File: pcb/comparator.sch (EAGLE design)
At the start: 13 parts, among them U1 MAX9032

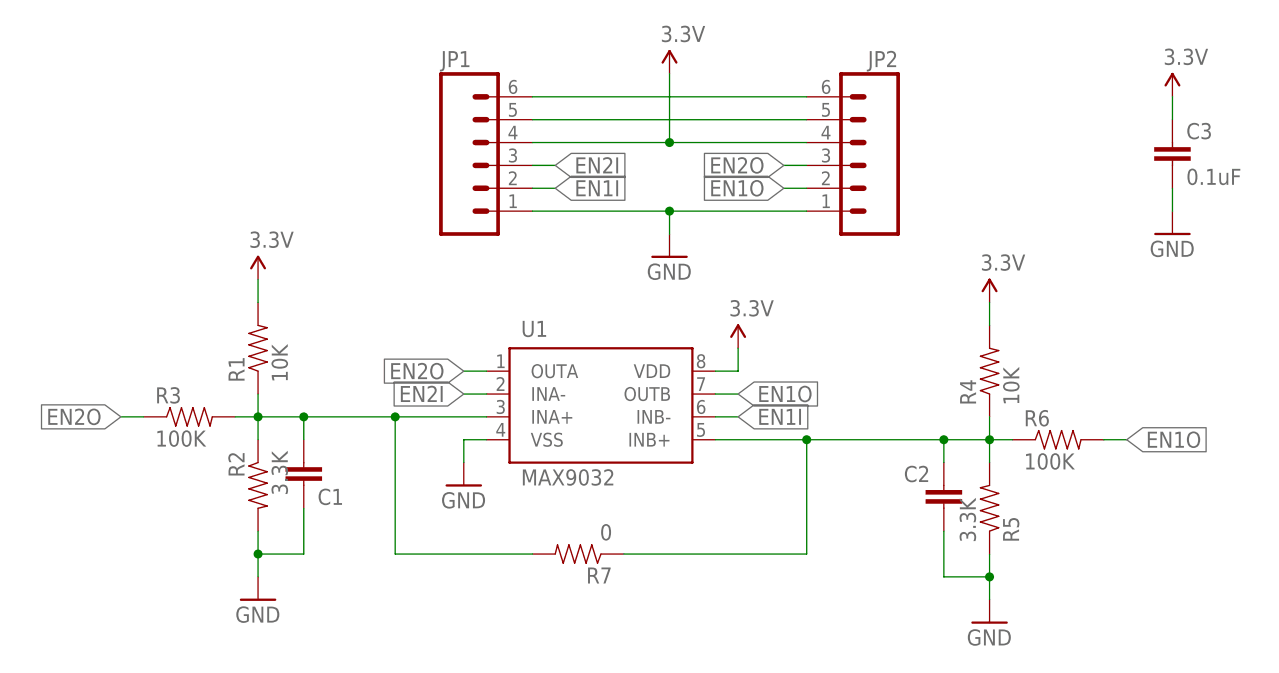
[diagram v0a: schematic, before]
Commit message: Tweaked encoder conditiner board
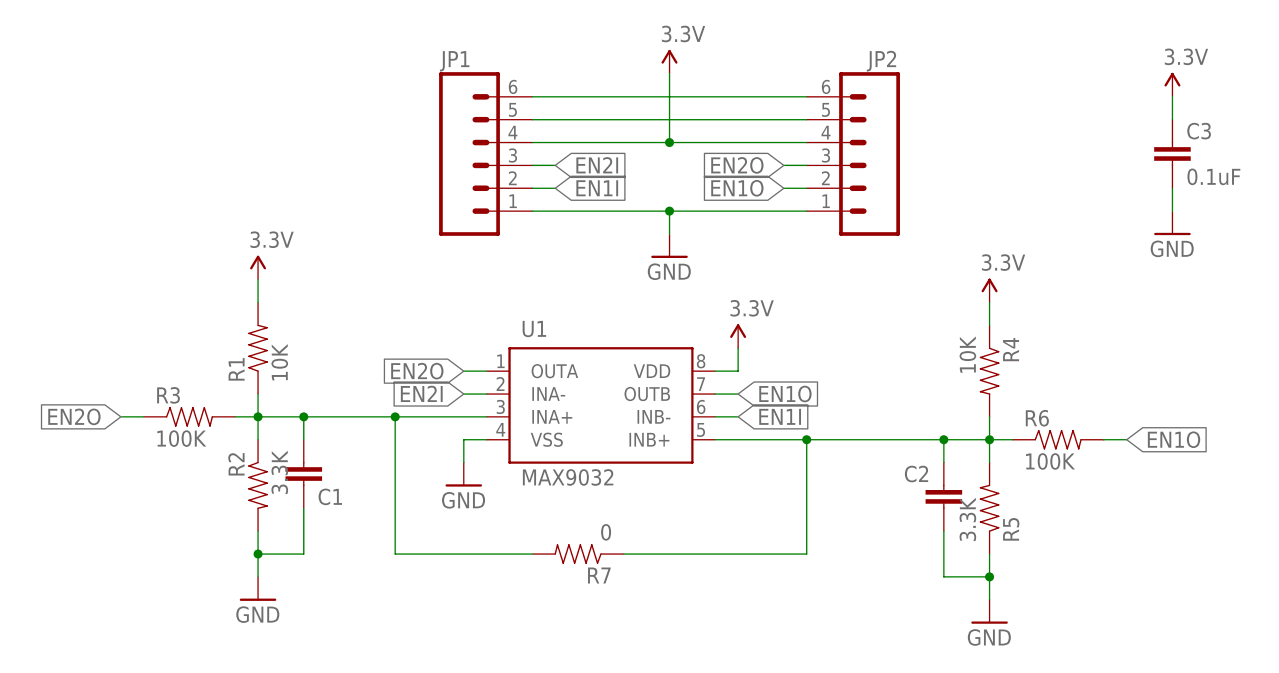
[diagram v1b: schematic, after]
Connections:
- net 3.3V: now also R4.1; no longer R4.2
- net N$6: now also R4.2; no longer R4.1
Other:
- moved on the sheet: R4
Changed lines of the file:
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@@
 <instance part="GND3" gate="1" x="5.08" y="15.24"/>
 <instance part="SUPPLY3" gate="G$1" x="5.08" y="50.8"/>
-<instance part="R4" gate="G$1" x="86.36" y="40.64" rot="R90"/>
+<instance part="R4" gate="G$1" x="86.36" y="40.64" rot="R270"/>
 <instance part="R5" gate="G$1" x="86.36" y="25.4" rot="MR90"/>
 <instance part="R6" gate="G$1" x="93.98" y="33.02"/>
@@
 </segment>
 <segment>
-<pinref part="R4" gate="G$1" pin="2"/>
+<pinref part="R4" gate="G$1" pin="1"/>
 <pinref part="SUPPLY4" gate="G$1" pin="3.3V"/>
 <wire x1="86.36" y1="48.26" x2="86.36" y2="45.72" width="0.1524" layer="91"/>
@@
 <pinref part="U1" gate="G$1" pin="INB+"/>
 <wire x1="88.9" y1="33.02" x2="86.36" y2="33.02" width="0.1524" layer="91"/>
-<pinref part="R4" gate="G$1" pin="1"/>
+<pinref part="R4" gate="G$1" pin="2"/>
 <pinref part="R5" gate="G$1" pin="2"/>
 <wire x1="86.36" y1="33.02" x2="81.28" y2="33.02" width="0.1524" layer="91"/>

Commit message: Specified capacitor value on comparator boards
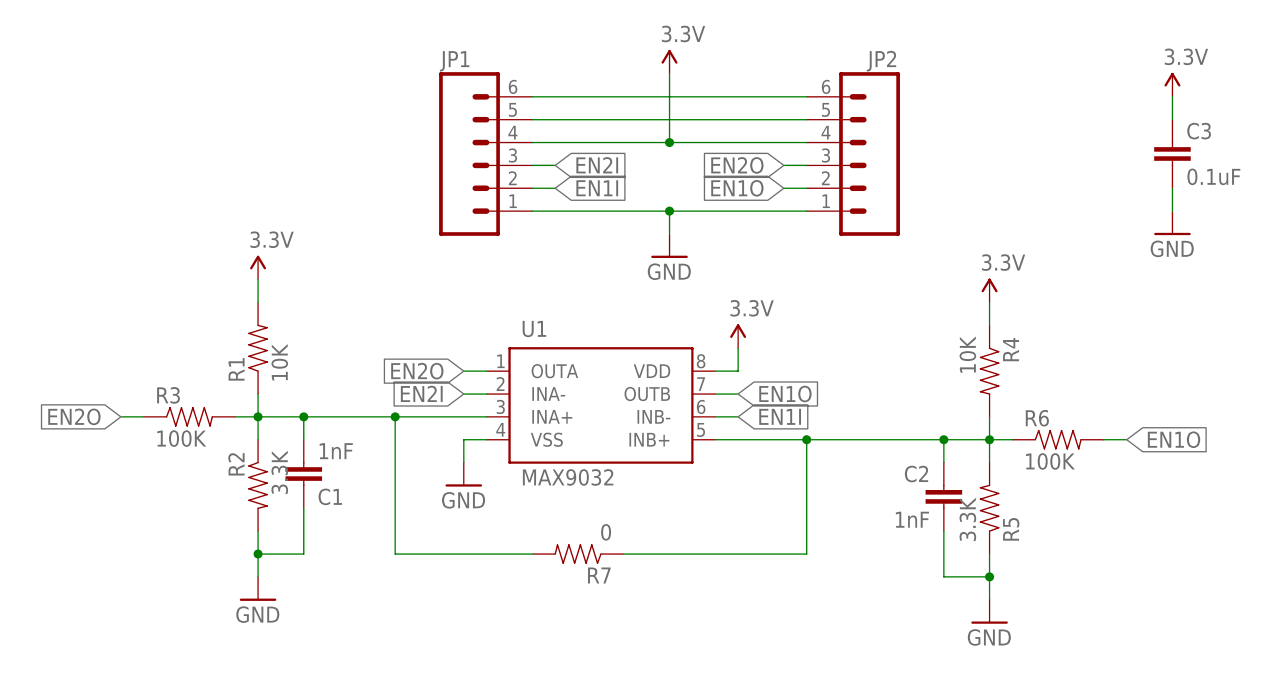
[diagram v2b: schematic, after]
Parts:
- C1, C2: value (none) -> 1nF
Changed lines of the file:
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@@
 <part name="SUPPLY4" library="SparkFun-Aesthetics" deviceset="3.3V" device=""/>
 <part name="GND4" library="SparkFun-Aesthetics" deviceset="GND" device=""/>
-<part name="C1" library="SparkFun-Capacitors" deviceset="CAP" device="0603-CAP"/>
-<part name="C2" library="SparkFun-Capacitors" deviceset="CAP" device="0603-CAP"/>
+<part name="C1" library="SparkFun-Capacitors" deviceset="CAP" device="0603-CAP" value="1nF"/>
+<part name="C2" library="SparkFun-Capacitors" deviceset="CAP" device="0603-CAP" value="1nF"/>
 <part name="C3" library="SparkFun-Capacitors" deviceset="CAP" device="0603-CAP" value="0.1uF"/>
 <part name="SUPPLY5" library="SparkFun-Aesthetics" deviceset="3.3V" device=""/>
